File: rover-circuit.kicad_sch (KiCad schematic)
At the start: 6 parts

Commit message: some progress
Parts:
- H1, H2, H3, H4: footprint MountingHole:MountingHole_2.2mm_M2_ISO14580 -> MountingHole:MountingHole_2.2mm_M2
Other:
- moved on the sheet: H1, H2

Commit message: progress on routing
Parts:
- added R16, R17: 4.7k, Resistor_SMD:R_0603_1608Metric, symbol Device:R
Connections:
- new net +3V3: R16.1, R17.1
- new net SCL: R17.2
- new net SDA: R16.2
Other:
- sheet Battery Recharger ports: added none; removed CD, PSEL, ~{INT}
- sheet IMU ports: added INT; removed none
- sheet MCU ports: added AIN1, AIN2, BIN1, BIN2, UWB_IRQ, UWB_RST, UWB_WUP, UWB_~{CS}, ~{SLEEP}; removed none

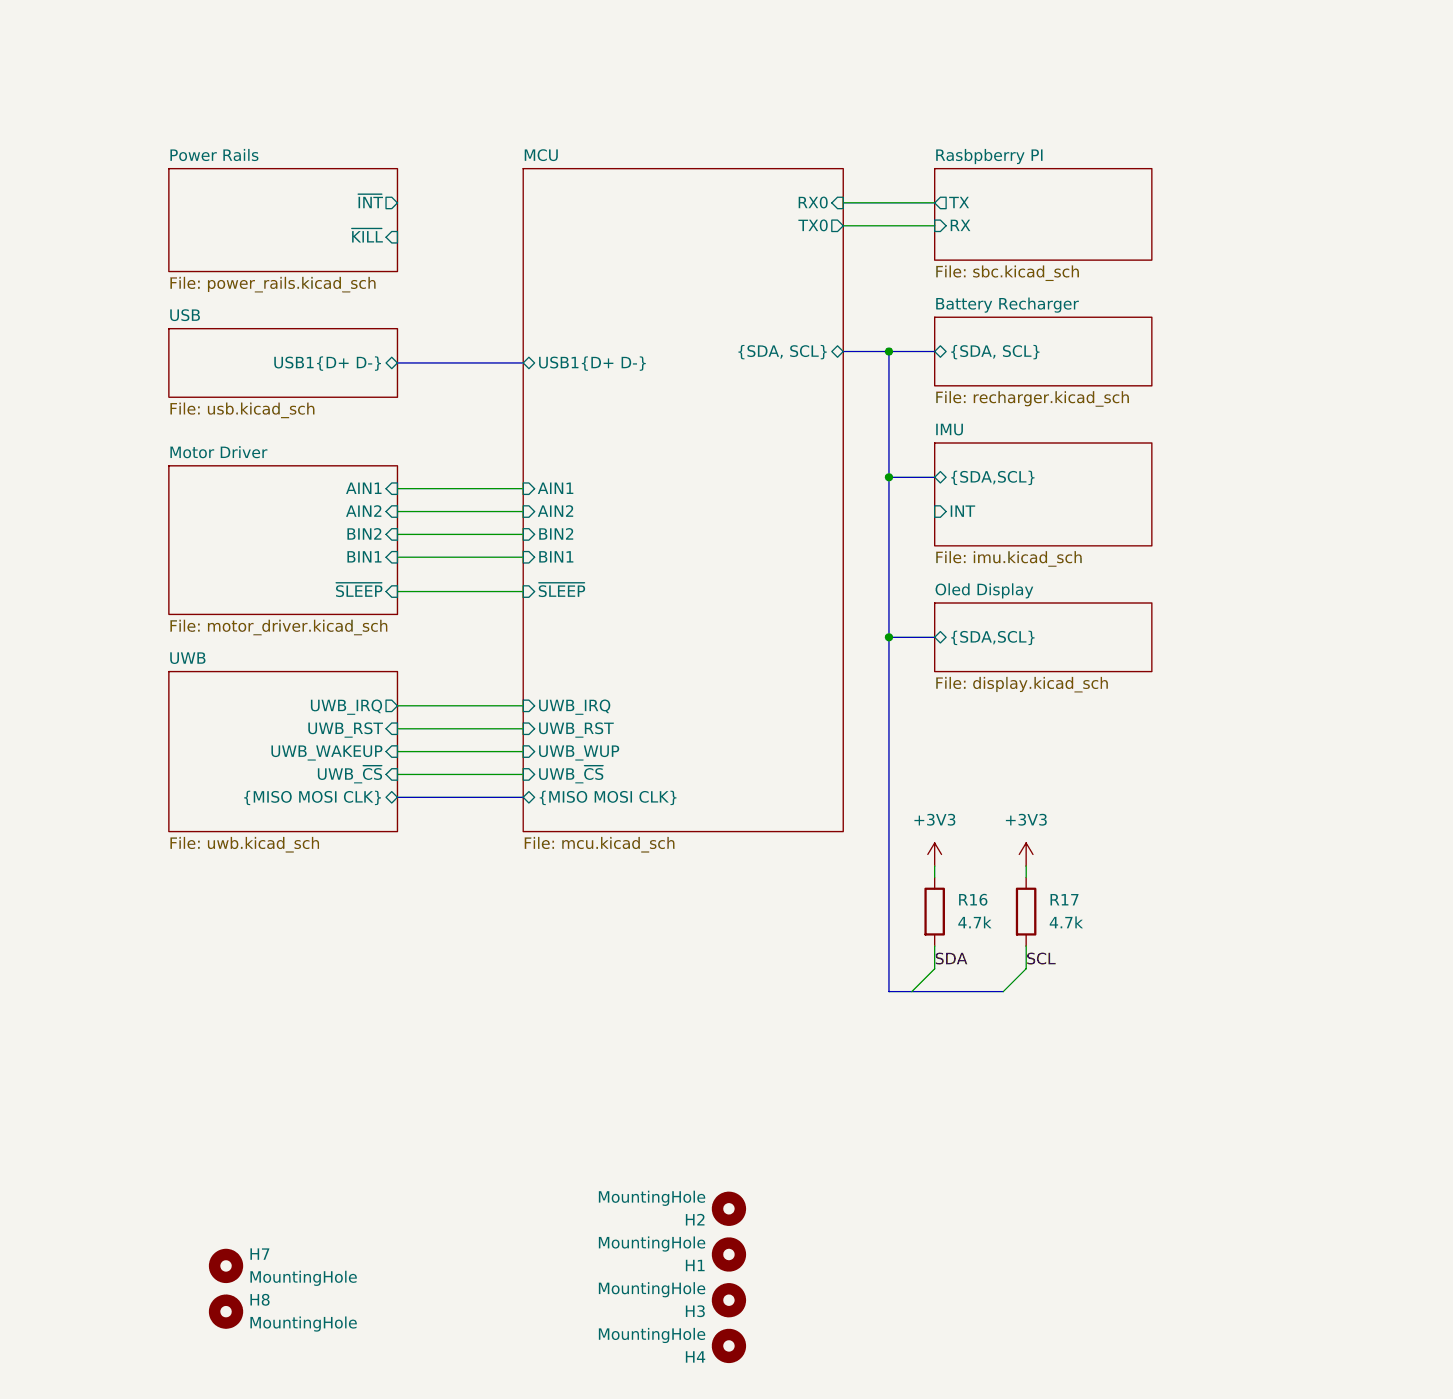
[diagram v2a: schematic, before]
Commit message: consolidated routing
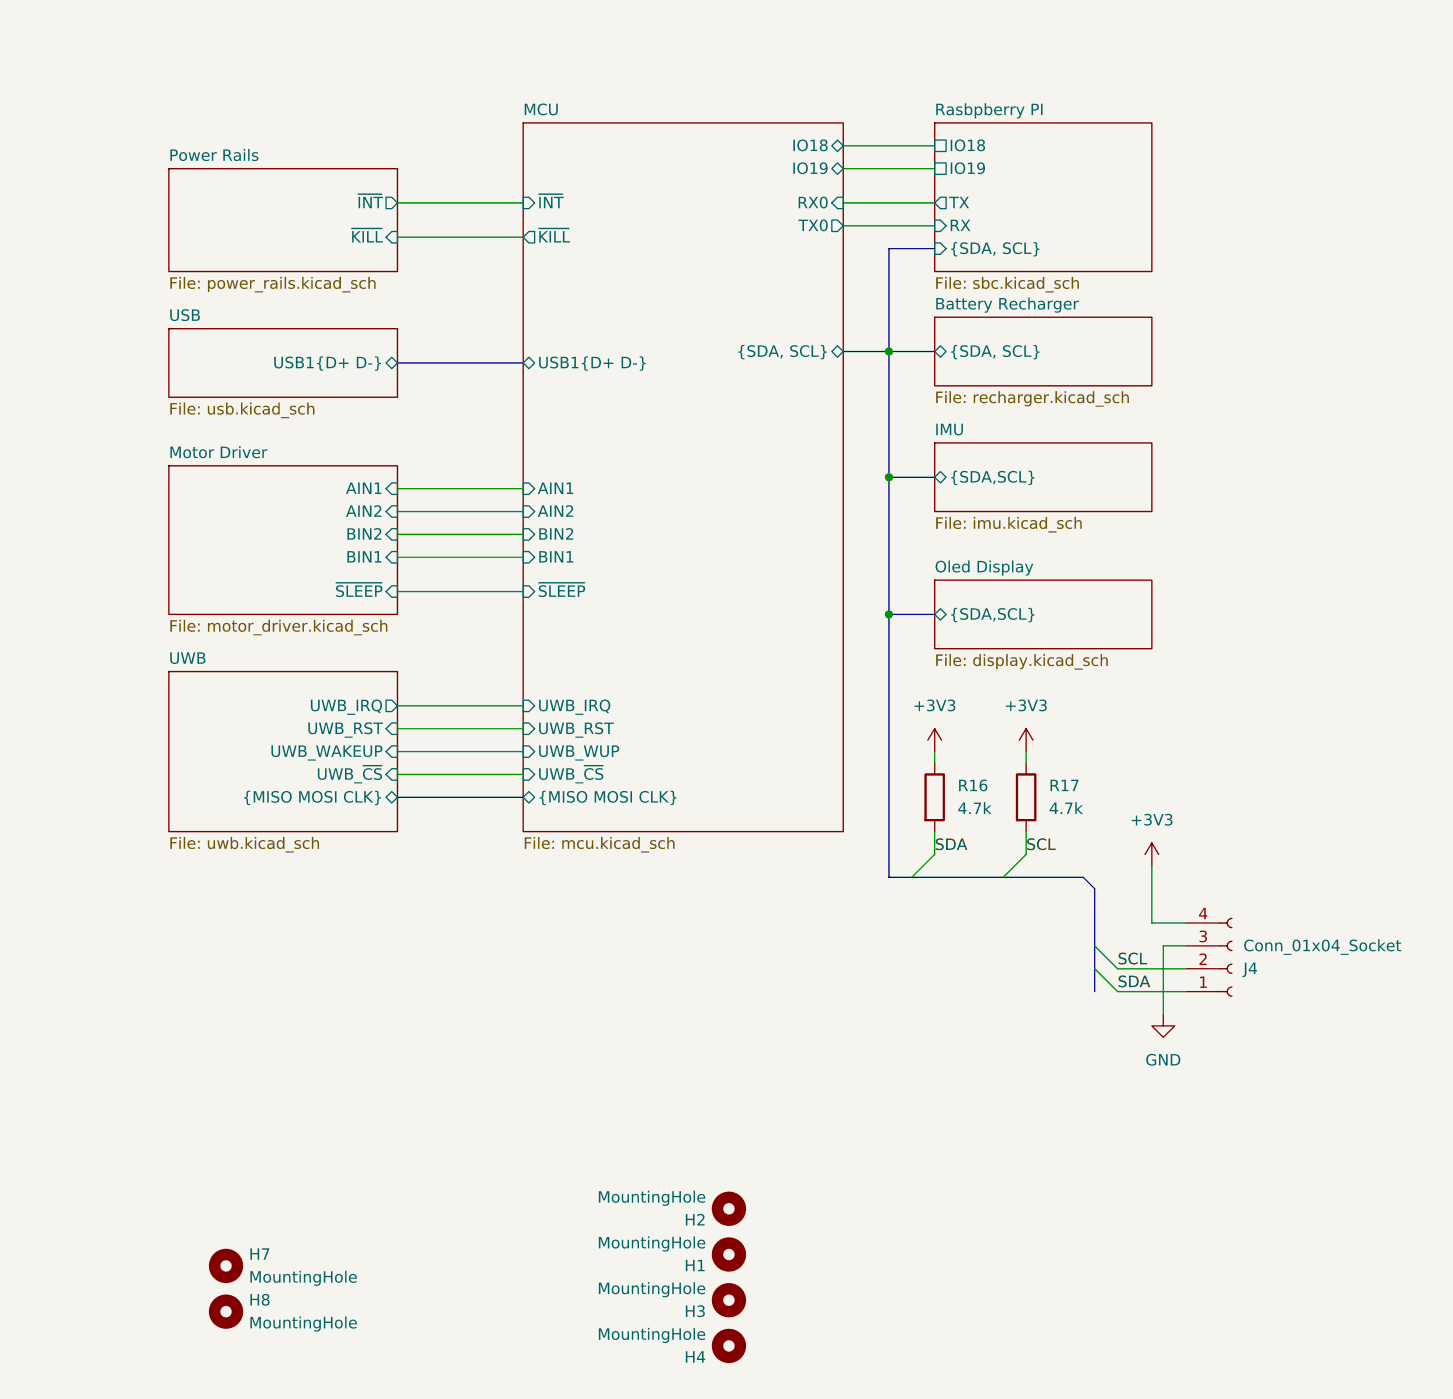
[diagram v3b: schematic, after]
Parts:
- added J4: Conn_01x04_Socket, Connector_JST:JST_PH_S4B-PH-SM4-TB_1x04-1MP_P2.00mm_Horizontal, symbol Connector:Conn_01x04_Socket
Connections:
- net +3V3: now also J4.4 (Pin_4)
- net SCL: now also J4.2 (Pin_2)
- net SDA: now also J4.1 (Pin_1)
- new net GND: J4.3 (Pin_3)
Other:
- sheet IMU ports: added none; removed INT
- sheet MCU ports: added IO18, IO19, ~{INT}, ~{KILL}; removed none
- sheet Rasbpberry PI ports: added IO18, IO19, {SDA, SCL}; removed none
- moved on the sheet: R16, R17

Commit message: improved routing
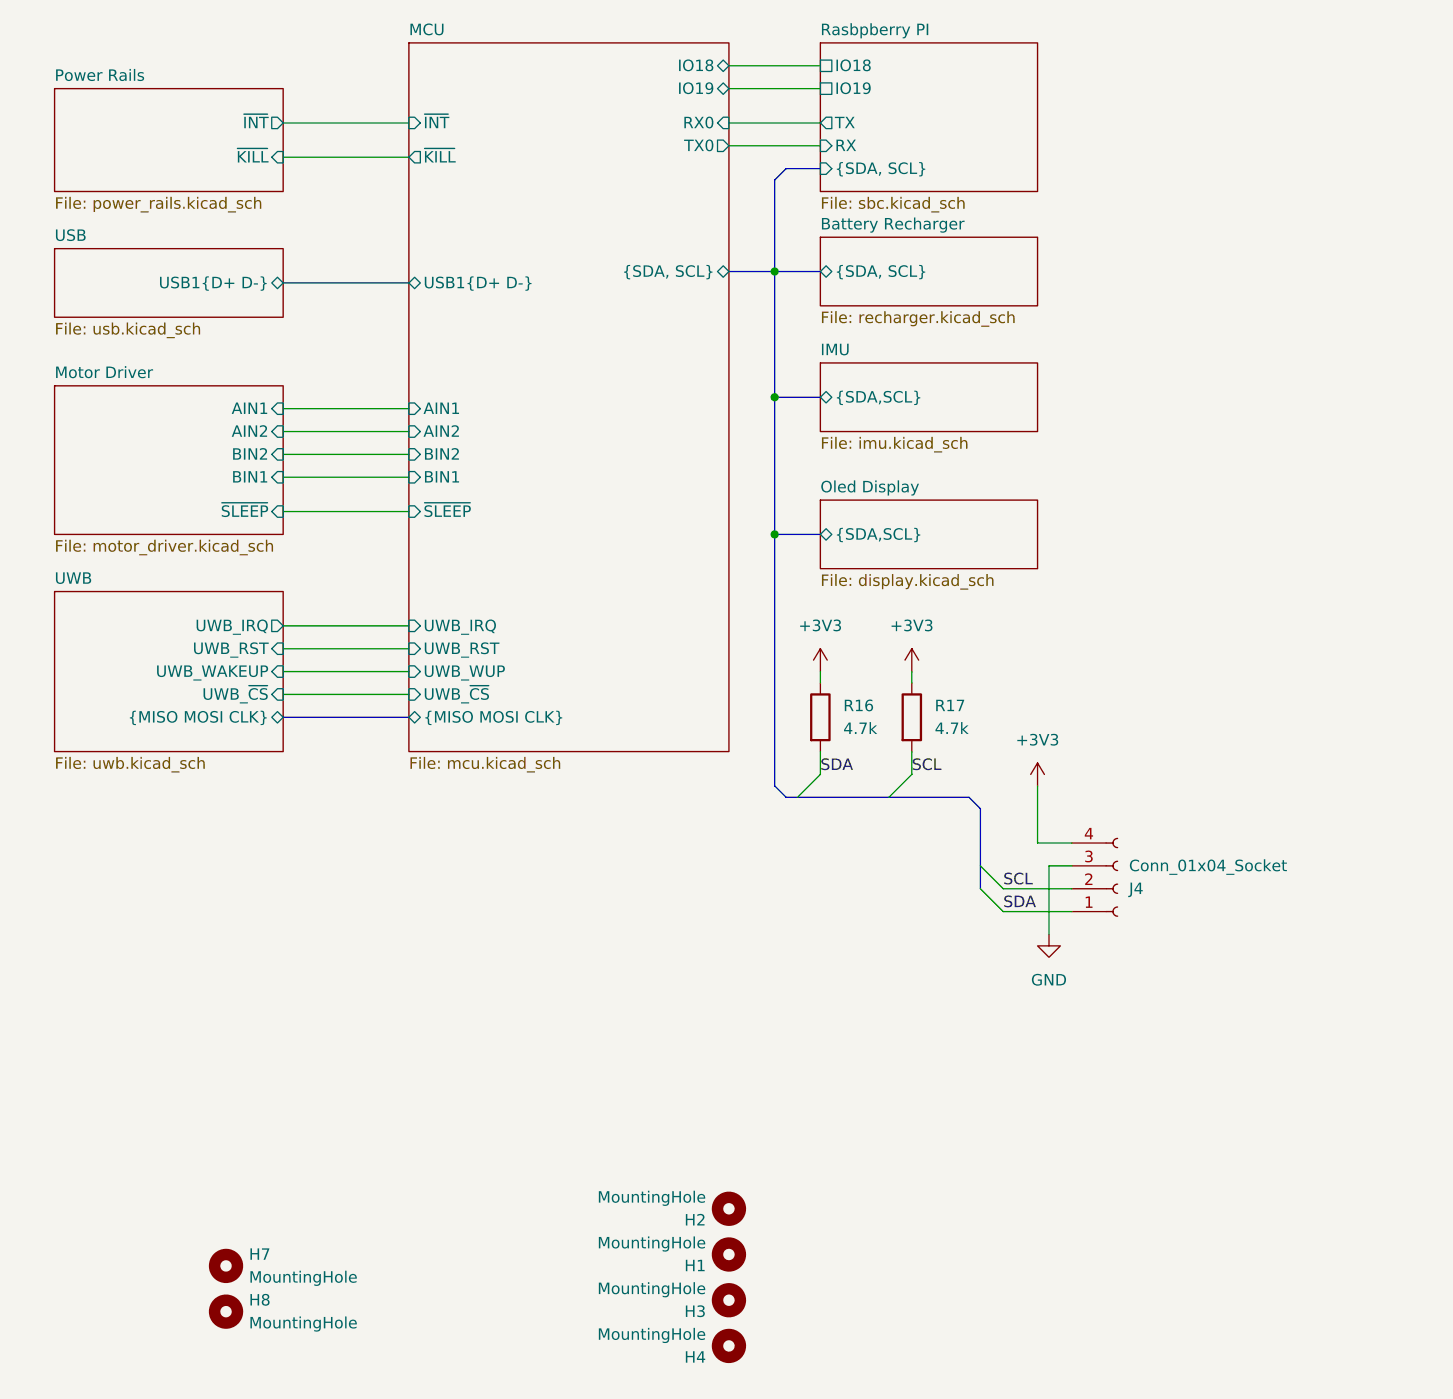
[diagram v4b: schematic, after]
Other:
- moved on the sheet: J4, R16, R17

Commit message: tentative automatic population
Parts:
- J4: LCSC (none) -> C265102; MPN (none) -> S4B-PH-SM4-TB(LF)(SN); Manufacturer (none) -> JST
- R16, R17: LCSC (none) -> C25999; MPN (none) -> 0603WAJ0472T5E; Manufacturer (none) -> UNI-ROYAL
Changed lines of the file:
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@@
 			)
 		)
-		(property "Datasheet" ""
+		(property "Datasheet" "https://datasheet.lcsc.com/datasheet/pdf/6c6fce4367275d84ec6a99bf09f1250f.pdf?productCode=C265102"
 			(at 200.66 139.7 0)
 			(hide yes)
@@
 					(size 1.27 1.27)
 				)
+			)
+		)
+		(property "Manufacturer" "JST" (at 0 0 0)
+			(effects
+				(font
+					(size 1.27 1.27)
+				)
+				(hide yes)
+			)
+		)
+		(property "MPN" "S4B-PH-SM4-TB(LF)(SN)" (at 0 0 0)
+			(effects
+				(font
+					(size 1.27 1.27)
+				)
+				(hide yes)
+			)
+		)
+		(property "LCSC" "C265102" (at 0 0 0)
+			(effects
+				(font
+					(size 1.27 1.27)
+				)
+				(hide yes)
 			)
 		)
@@
 			)
 		)
-		(property "Datasheet" ""
+		(property "Datasheet" "https://datasheet.lcsc.com/datasheet/pdf/0a975aaa49b7c97f38a963127be4a823.pdf?productCode=C25999"
 			(at 177.8 120.65 0)
 			(hide yes)
@@
 					(size 1.27 1.27)
 				)
+			)
+		)
+		(property "Manufacturer" "UNI-ROYAL" (at 0 0 0)
+			(effects
+				(font
+					(size 1.27 1.27)
+				)
+				(hide yes)
+			)
+		)
+		(property "MPN" "0603WAJ0472T5E" (at 0 0 0)
+			(effects
+				(font
+					(size 1.27 1.27)
+				)
+				(hide yes)
+			)
+		)
+		(property "LCSC" "C25999" (at 0 0 0)
+			(effects
+				(font
+					(size 1.27 1.27)
+				)
+				(hide yes)
 			)
 		)
@@
 			)
 		)
-		(property "Datasheet" ""
+		(property "Datasheet" "https://datasheet.lcsc.com/datasheet/pdf/0a975aaa49b7c97f38a963127be4a823.pdf?productCode=C25999"
 			(at 167.64 120.65 0)
 			(hide yes)
@@
 			)
 		)
+		(property "Manufacturer" "UNI-ROYAL" (at 0 0 0)
+			(effects
+				(font
+					(size 1.27 1.27)
+				)
+				(hide yes)
+			)
+		)
+		(property "MPN" "0603WAJ0472T5E" (at 0 0 0)
+			(effects
+				(font
+					(size 1.27 1.27)
+				)
+				(hide yes)
+			)
+		)
+		(property "LCSC" "C25999" (at 0 0 0)
+			(effects
+				(font
+					(size 1.27 1.27)
+				)
+				(hide yes)
+			)
+		)

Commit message: Consistent final layout
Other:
- sheet Power Rails ports: added HOLD, PB_OUT; removed ~{INT}, ~{KILL}
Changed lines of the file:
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@@
+		)
+	)
+	(bus
+		(pts
+			(xy 162.56 100.33) (xy 167.64 100.33)
+		)
+		(stroke
+			(width 0)
+			(type default)
+		)
+	)
+	(bus
+		(pts
+			(xy 184.15 129.54) (xy 185.42 130.81)
+		)
+		(stroke
+			(width 0)
+			(type default)
 		)
 	)
 	(wire
 		(pts
+			(xy 107.95 118.11) (xy 121.92 118.11)
+		)
+		(stroke
+			(width 0)
+			(type default)
+		)
+	)
+	(bus
+		(pts
+			(xy 162.56 71.12) (xy 167.64 71.12)
+		)
+		(stroke
+			(width 0)
+			(type default)
+		)
+	)
+	(wire
+		(pts
+			(xy 107.95 88.9) (xy 121.92 88.9)
+		)
+		(stroke
+			(width 0)
+			(type default)
+		)
+	)
+	(wire
+		(pts
+			(xy 177.8 115.57) (xy 177.8 116.84)
+		)
+		(stroke
+			(width 0)
+			(type default)
+		)
+	)
+	(wire
+		(pts
 			(xy 107.95 58.42) (xy 121.92 58.42)
 		)
@@
 		)
 	)
+	(bus
+		(pts
+			(xy 163.83 129.54) (xy 162.56 128.27)
+		)
+		(stroke
+			(width 0)
+			(type default)
+		)
+	)
+	(bus
+		(pts
+			(xy 107.95 72.39) (xy 121.92 72.39)
+		)
+		(stroke
+			(width 0)
+			(type default)
+		)
+	)
 	(wire
 		(pts
+			(xy 187.96 142.24) (xy 195.58 142.24)
+		)
+		(stroke
+			(width 0)
+			(type default)
+		)
+	)
+	(bus
+		(pts
+			(xy 162.56 85.09) (xy 162.56 100.33)
+		)
+		(stroke
+			(width 0)
+			(type default)
+		)
+	)
+	(wire
+		(pts
 			(xy 107.95 54.61) (xy 121.92 54.61)
-		)
-		(stroke
-			(width 0)
-			(type default)
-		)
-	)
-	(bus
-		(pts
-			(xy 162.56 100.33) (xy 167.64 100.33)
-		)
-		(stroke
-			(width 0)
-			(type default)
-		)
-	)
-	(bus
-		(pts
-			(xy 184.15 129.54) (xy 185.42 130.81)
-		)
-		(stroke
-			(width 0)
-			(type default)
-		)
-	)
-	(wire
-		(pts
-			(xy 107.95 118.11) (xy 121.92 118.11)
-		)
-		(stroke
-			(width 0)
-			(type default)
-		)
-	)
-	(bus
-		(pts
-			(xy 162.56 71.12) (xy 167.64 71.12)
-		)
-		(stroke
-			(width 0)
-			(type default)
-		)
-	)
-	(wire
-		(pts
-			(xy 107.95 88.9) (xy 121.92 88.9)
-		)
-		(stroke
-			(width 0)
-			(type default)
-		)
-	)
-	(wire
-		(pts
-			(xy 177.8 115.57) (xy 177.8 116.84)
-		)
-		(stroke
-			(width 0)
-			(type default)
-		)
-	)
-	(bus
-		(pts
-			(xy 163.83 129.54) (xy 162.56 128.27)
-		)
-		(stroke
-			(width 0)
-			(type default)
-		)
-	)
-	(bus
-		(pts
-			(xy 107.95 72.39) (xy 121.92 72.39)
-		)
-		(stroke
-			(width 0)
-			(type default)
-		)
-	)
-	(wire
-		(pts
-			(xy 187.96 142.24) (xy 195.58 142.24)
-		)
-		(stroke
-			(width 0)
-			(type default)
-		)
-	)
-	(bus
-		(pts
-			(xy 162.56 85.09) (xy 162.56 100.33)
 		)
 		(stroke
@@
 			)
 		)
-		(property "Manufacturer" "JST" (at 0 0 0)
-			(effects
-				(font
-					(size 1.27 1.27)
-				)
-				(hide yes)
-			)
-		)
-		(property "MPN" "S4B-PH-SM4-TB(LF)(SN)" (at 0 0 0)
-			(effects
-				(font
-					(size 1.27 1.27)
-				)
-				(hide yes)
-			)
-		)
-		(property "LCSC" "C265102" (at 0 0 0)
-			(effects
-				(font
-					(size 1.27 1.27)
-				)
-				(hide yes)
+		(property "Manufacturer" "JST"
+			(at 0 0 0)
+			(hide yes)
+			(show_name no)
+			(do_not_autoplace no)
+			(effects
+				(font
+					(size 1.27 1.27)
+				)
+			)
+		)
+		(property "MPN" "S4B-PH-SM4-TB(LF)(SN)"
+			(at 0 0 0)
+			(hide yes)
+			(show_name no)
+			(do_not_autoplace no)
+			(effects
+				(font
+					(size 1.27 1.27)
+				)
+			)
+		)
+		(property "LCSC" "C265102"
+			(at 0 0 0)
+			(hide yes)
+			(show_name no)
+			(do_not_autoplace no)
+			(effects
+				(font
+					(size 1.27 1.27)
+				)
 			)
 		)
@@
 			)
 		)
-		(property "Manufacturer" "UNI-ROYAL" (at 0 0 0)
-			(effects
-				(font
-					(size 1.27 1.27)
-				)
-				(hide yes)
-			)
-		)
-		(property "MPN" "0603WAJ0472T5E" (at 0 0 0)
-			(effects
-				(font
-					(size 1.27 1.27)
-				)
-				(hide yes)
-			)
-		)
-		(property "LCSC" "C25999" (at 0 0 0)
-			(effects
-				(font
-					(size 1.27 1.27)
-				)
-				(hide yes)
+		(property "Manufacturer" "UNI-ROYAL"
+			(at 0 0 0)
+			(hide yes)
+			(show_name no)
+			(do_not_autoplace no)
+			(effects
+				(font
+					(size 1.27 1.27)
+				)
+			)
+		)
+		(property "MPN" "0603WAJ0472T5E"
+			(at 0 0 0)
+			(hide yes)
+			(show_name no)
+			(do_not_autoplace no)
+			(effects
+				(font
+					(size 1.27 1.27)
+				)
+			)
+		)
+		(property "LCSC" "C25999"
+			(at 0 0 0)
+			(hide yes)
+			(show_name no)
+			(do_not_autoplace no)
+			(effects
+				(font
+					(size 1.27 1.27)
+				)
 			)
 		)
@@
 			)
 		)
-		(property "Manufacturer" "UNI-ROYAL" (at 0 0 0)
-			(effects
-				(font
-					(size 1.27 1.27)
-				)
-				(hide yes)
-			)
-		)
-		(property "MPN" "0603WAJ0472T5E" (at 0 0 0)
-			(effects
-				(font
-					(size 1.27 1.27)
-				)
-				(hide yes)
-			)
-		)
-		(property "LCSC" "C25999" (at 0 0 0)
-			(effects
-				(font
-					(size 1.27 1.27)
-				)
-				(hide yes)
+		(property "Manufacturer" "UNI-ROYAL"
+			(at 0 0 0)
+			(hide yes)
+			(show_name no)
+			(do_not_autoplace no)
+			(effects
+				(font
+					(size 1.27 1.27)
+				)
+			)
+		)
+		(property "MPN" "0603WAJ0472T5E"
+			(at 0 0 0)
+			(hide yes)
+			(show_name no)
+			(do_not_autoplace no)
+			(effects
+				(font
+					(size 1.27 1.27)
+				)
+			)
+		)
+		(property "LCSC" "C25999"
+			(at 0 0 0)
+			(hide yes)
+			(show_name no)
+			(do_not_autoplace no)
+			(effects
+				(font
+					(size 1.27 1.27)
+				)
 			)
 		)
@@
 			)
 		)
-		(pin "~{INT}" output
+		(pin "HOLD" input
+			(at 107.95 58.42 0)
+			(effects
+				(font
+					(size 1.27 1.27)
+				)
+				(justify right)
+			)
+		)
+		(pin "PB_OUT" output
 			(at 107.95 54.61 0)
 			(effects
 				(font
-					(size 1.27 1.27)
-				)
-				(justify right)
-			)
-		)
-		(pin "~{KILL}" input
-			(at 107.95 58.42 0)
-			(effects
-				(font
